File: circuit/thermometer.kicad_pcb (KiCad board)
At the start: 2 copper layers, 1 part, among them IC1 ICL7107CPL

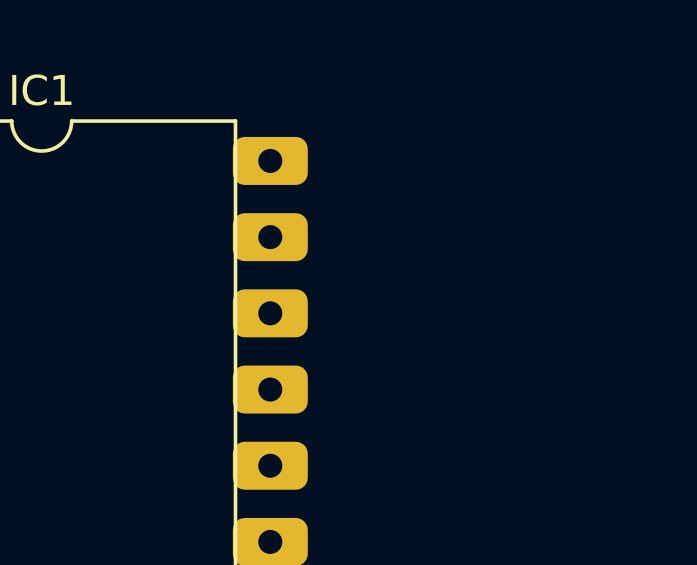
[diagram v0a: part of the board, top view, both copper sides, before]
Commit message: Configure oscillator
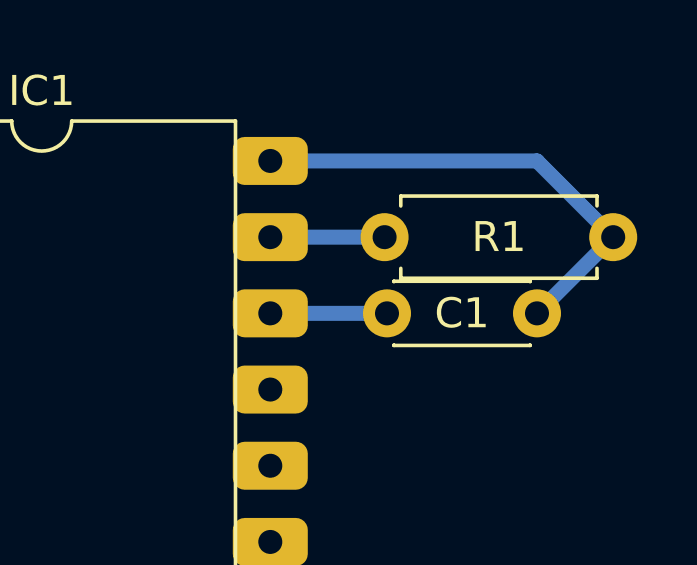
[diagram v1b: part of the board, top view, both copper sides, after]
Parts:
- added C1: 100pF, Capacitor_THT:C_Disc_D4.3mm_W1.9mm_P5.00mm, F.Cu at (101.7, 81.3)
- added R1: 100k, Resistor_THT:R_Axial_DIN0207_L6.3mm_D2.5mm_P7.62mm_Horizontal, F.Cu at (101.6, 78.7)
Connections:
- IC1 pad 38: unconnected-(IC1-OSC3-Pad38) -> Net-(IC1-OSC3)
- IC1 pad 39: unconnected-(IC1-OSC2-Pad39) -> Net-(IC1-OSC2)
- IC1 pad 40: unconnected-(IC1-OSC1-Pad40) -> Net-(IC1-OSC1)
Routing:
- net Net-(IC1-OSC1): track 0.00 -> 16.1 mm
- net Net-(IC1-OSC3): track 0.00 -> 3.89 mm
- net Net-(IC1-OSC2): track 0.00 -> 3.81 mm
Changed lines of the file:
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@@
   (net 36 "unconnected-(IC1-REF_HI-Pad36)")
   (net 37 "unconnected-(IC1-TEST-Pad37)")
-  (net 38 "unconnected-(IC1-OSC3-Pad38)")
-  (net 39 "unconnected-(IC1-OSC2-Pad39)")
-  (net 40 "unconnected-(IC1-OSC1-Pad40)")
+  (net 38 "Net-(IC1-OSC3)")
+  (net 39 "Net-(IC1-OSC1)")
+  (net 40 "Net-(IC1-OSC2)")
   (footprint "Package_DIP:DIP-40_W15.24mm" (layer "F.Cu")
     (at 82.55 76.2)
@@
       (net 37 "unconnected-(IC1-TEST-Pad37)") (pinfunction "TEST") (pintype "passive"))
     (pad "38" thru_hole roundrect (at 15.24 5.08) (size 2.5 1.6) (drill 0.8) (layers "*.Cu" "*.Mask") (roundrect_rratio 0.25)
-      (net 38 "unconnected-(IC1-OSC3-Pad38)") (pinfunction "OSC3") (pintype "passive"))
+      (net 38 "Net-(IC1-OSC3)") (pinfunction "OSC3") (pintype "passive"))
     (pad "39" thru_hole roundrect (at 15.24 2.54) (size 2.5 1.6) (drill 0.8) (layers "*.Cu" "*.Mask") (roundrect_rratio 0.25)
-      (net 39 "unconnected-(IC1-OSC2-Pad39)") (pinfunction "OSC2") (pintype "passive"))
+      (net 40 "Net-(IC1-OSC2)") (pinfunction "OSC2") (pintype "passive"))
     (pad "40" thru_hole roundrect (at 15.24 0) (size 2.5 1.6) (drill 0.8) (layers "*.Cu" "*.Mask") (roundrect_rratio 0.25)
-      (net 40 "unconnected-(IC1-OSC1-Pad40)") (pinfunction "OSC1") (pintype "passive"))
+      (net 39 "Net-(IC1-OSC1)") (pinfunction "OSC1") (pintype "passive"))
     (model "${KICAD6_3DMODEL_DIR}/Package_DIP.3dshapes/DIP-40_W15.24mm.wrl"
       (offset (xyz 0 0 0))
@@
     )
   )
+  (footprint "Capacitor_THT:C_Disc_D4.3mm_W1.9mm_P5.00mm" (layer "F.Cu")
+    (at 101.68 81.28)
+    (descr "C, Disc series, Radial, pin pitch=5.00mm, , diameter*width=4.3*1.9mm^2, Capacitor, http://www.vishay.com/docs/45233/krseries.pdf")
+    (tags "C Disc series Radial pin pitch 5.00mm  diameter 4.3mm width 1.9mm Capacitor")
+    (property "Sheetfile" "thermometer.kicad_sch")
+    (property "Sheetname" "")
+    (property "ki_description" "Unpolarized capacitor")
+    (property "ki_keywords" "cap capacitor")
+    (attr through_hole)
+    (fp_text reference "C1" (at 2.5 0) (layer "F.SilkS")
+        (effects (font (size 1 1) (thickness 0.15)))
+    )
+    (fp_text value "100pF" (at 2.5 2.2) (layer "F.Fab")
+        (effects (font (size 1 1) (thickness 0.15)))
+    )
+    (fp_text user "${REFERENCE}" (at 2.5 0) (layer "F.Fab")
+        (effects (font (size 0.86 0.86) (thickness 0.129)))
+    )
+    (fp_line (start 0.23 -1.07) (end 0.23 -1.055)
+      (stroke (width 0.12) (type solid)) (layer "F.SilkS"))
+    (fp_line (start 0.23 -1.07) (end 4.77 -1.07)
+      (stroke (width 0.12) (type solid)) (layer "F.SilkS"))
+    (fp_line (start 0.23 1.055) (end 0.23 1.07)
+      (stroke (width 0.12) (type solid)) (layer "F.SilkS"))
+    (fp_line (start 0.23 1.07) (end 4.77 1.07)
+      (stroke (width 0.12) (type solid)) (layer "F.SilkS"))
+    (fp_line (start 4.77 -1.07) (end 4.77 -1.055)
+      (stroke (width 0.12) (type solid)) (layer "F.SilkS"))
+    (fp_line (start 4.77 1.055) (end 4.77 1.07)
+      (stroke (width 0.12) (type solid)) (layer "F.SilkS"))
+    (fp_line (start -1.05 -1.2) (end -1.05 1.2)
+      (stroke (width 0.05) (type solid)) (layer "F.CrtYd"))
+    (fp_line (start -1.05 1.2) (end 6.05 1.2)
+      (stroke (width 0.05) (type solid)) (layer "F.CrtYd"))
+    (fp_line (start 6.05 -1.2) (end -1.05 -1.2)
+      (stroke (width 0.05) (type solid)) (layer "F.CrtYd"))
+    (fp_line (start 6.05 1.2) (end 6.05 -1.2)
+      (stroke (width 0.05) (type solid)) (layer "F.CrtYd"))
+    (fp_line (start 0.35 -0.95) (end 0.35 0.95)
+      (stroke (width 0.1) (type solid)) (layer "F.Fab"))
+    (fp_line (start 0.35 0.95) (end 4.65 0.95)
+      (stroke (width 0.1) (type solid)) (layer "F.Fab"))
+    (fp_line (start 4.65 -0.95) (end 0.35 -0.95)
+      (stroke (width 0.1) (type solid)) (layer "F.Fab"))
+    (fp_line (start 4.65 0.95) (end 4.65 -0.95)
+      (stroke (width 0.1) (type solid)) (layer "F.Fab"))
+    (pad "1" thru_hole circle (at 0 0) (size 1.6 1.6) (drill 0.8) (layers "*.Cu" "*.Mask")
+      (net 38 "Net-(IC1-OSC3)") (pintype "passive"))
+    (pad "2" thru_hole circle (at 5 0) (size 1.6 1.6) (drill 0.8) (layers "*.Cu" "*.Mask")
+      (net 39 "Net-(IC1-OSC1)") (pintype "passive"))
+    (model "${KICAD6_3DMODEL_DIR}/Capacitor_THT.3dshapes/C_Disc_D4.3mm_W1.9mm_P5.00mm.wrl"
+      (offset (xyz 0 0 0))
+      (scale (xyz 1 1 1))
+      (rotate (xyz 0 0 0))
+    )
+  )
+  (footprint "Resistor_THT:R_Axial_DIN0207_L6.3mm_D2.5mm_P7.62mm_Horizontal" (layer "F.Cu")
+    (at 101.6 78.74)
+    (descr "Resistor, Axial_DIN0207 series, Axial, Horizontal, pin pitch=7.62mm, 0.25W = 1/4W, length*diameter=6.3*2.5mm^2, http://cdn-reichelt.de/documents/datenblatt/B400/1_4W%23YAG.pdf")
+    (tags "Resistor Axial_DIN0207 series Axial Horizontal pin pitch 7.62mm 0.25W = 1/4W length 6.3mm diameter 2.5mm")
+    (property "Sheetfile" "thermometer.kicad_sch")
+    (property "Sheetname" "")
+    (property "ki_description" "Resistor, US symbol")
+    (property "ki_keywords" "R res resistor")
+    (attr through_hole)
+    (fp_text reference "R1" (at 3.81 0) (layer "F.SilkS")
+        (effects (font (size 1 1) (thickness 0.15)))
+    )
+    (fp_text value "100k" (at 3.81 2.37) (layer "F.Fab")
+        (effects (font (size 1 1) (thickness 0.15)))
+    )
+    (fp_text user "${REFERENCE}" (at 3.81 0) (layer "F.Fab")
+        (effects (font (size 1 1) (thickness 0.15)))
+    )
+    (fp_line (start 0.54 -1.37) (end 7.08 -1.37)
+      (stroke (width 0.12) (type solid)) (layer "F.SilkS"))
+    (fp_line (start 0.54 -1.04) (end 0.54 -1.37)
+      (stroke (width 0.12) (type solid)) (layer "F.SilkS"))
+    (fp_line (start 0.54 1.04) (end 0.54 1.37)
+      (stroke (width 0.12) (type solid)) (layer "F.SilkS"))
+    (fp_line (start 0.54 1.37) (end 7.08 1.37)
+      (stroke (width 0.12) (type solid)) (layer "F.SilkS"))
+    (fp_line (start 7.08 -1.37) (end 7.08 -1.04)
+      (stroke (width 0.12) (type solid)) (layer "F.SilkS"))
+    (fp_line (start 7.08 1.37) (end 7.08 1.04)
+      (stroke (width 0.12) (type solid)) (layer "F.SilkS"))
+    (fp_line (start -1.05 -1.5) (end -1.05 1.5)
+      (stroke (width 0.05) (type solid)) (layer "F.CrtYd"))
+    (fp_line (start -1.05 1.5) (end 8.67 1.5)
+      (stroke (width 0.05) (type solid)) (layer "F.CrtYd"))
+    (fp_line (start 8.67 -1.5) (end -1.05 -1.5)
+      (stroke (width 0.05) (type solid)) (layer "F.CrtYd"))
+    (fp_line (start 8.67 1.5) (end 8.67 -1.5)
+      (stroke (width 0.05) (type solid)) (layer "F.CrtYd"))
+    (fp_line (start 0 0) (end 0.66 0)
+      (stroke (width 0.1) (type solid)) (layer "F.Fab"))
+    (fp_line (start 0.66 -1.25) (end 0.66 1.25)
+      (stroke (width 0.1) (type solid)) (layer "F.Fab"))
+    (fp_line (start 0.66 1.25) (end 6.96 1.25)
+      (stroke (width 0.1) (type solid)) (layer "F.Fab"))
+    (fp_line (start 6.96 -1.25) (end 0.66 -1.25)
+      (stroke (width 0.1) (type solid)) (layer "F.Fab"))
+    (fp_line (start 6.96 1.25) (end 6.96 -1.25)
+      (stroke (width 0.1) (type solid)) (layer "F.Fab"))
+    (fp_line (start 7.62 0) (end 6.96 0)
+      (stroke (width 0.1) (type solid)) (layer "F.Fab"))
+    (pad "1" thru_hole circle (at 0 0) (size 1.6 1.6) (drill 0.8) (layers "*.Cu" "*.Mask")
+      (net 40 "Net-(IC1-OSC2)") (pintype "passive"))
+    (pad "2" thru_hole oval (at 7.62 0) (size 1.6 1.6) (drill 0.8) (layers "*.Cu" "*.Mask")
+      (net 39 "Net-(IC1-OSC1)") (pintype "passive"))
+    (model "${KICAD6_3DMODEL_DIR}/Resistor_THT.3dshapes/R_Axial_DIN0207_L6.3mm_D2.5mm_P7.62mm_Horizontal.wrl"
+      (offset (xyz 0 0 0))
+      (scale (xyz 1 1 1))
+      (rotate (xyz 0 0 0))
+    )
+  )
+  (segment (start 97.79 81.28) (end 101.68 81.28) (width 0.5) (layer "B.Cu") (net 38))
+  (segment (start 106.68 81.28) (end 109.22 78.74) (width 0.5) (layer "B.Cu") (net 39))
+  (segment (start 97.79 76.2) (end 106.68 76.2) (width 0.5) (layer "B.Cu") (net 39))
+  (segment (start 106.68 76.2) (end 109.22 78.74) (width 0.5) (layer "B.Cu") (net 39))
+  (segment (start 97.79 78.74) (end 101.6 78.74) (width 0.5) (layer "B.Cu") (net 40))
 )

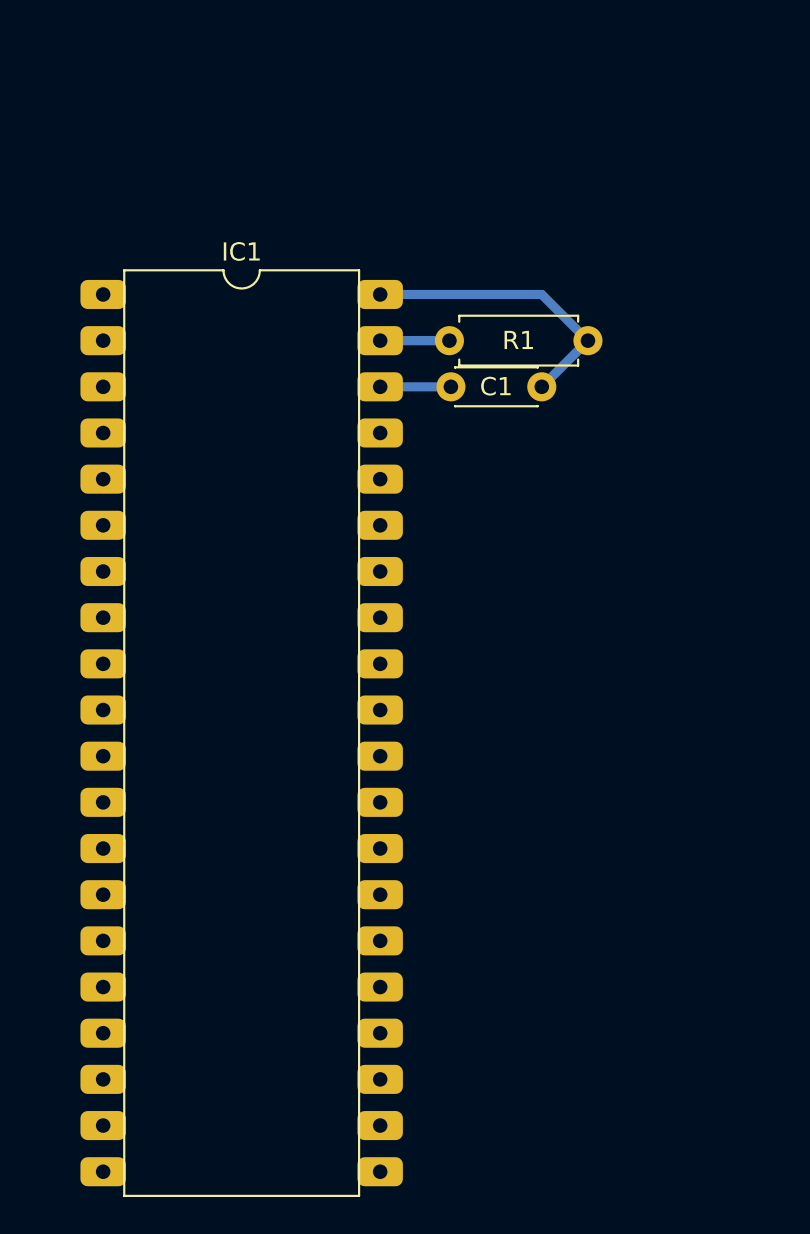
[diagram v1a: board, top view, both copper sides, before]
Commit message: Place all remaining thermometer parts
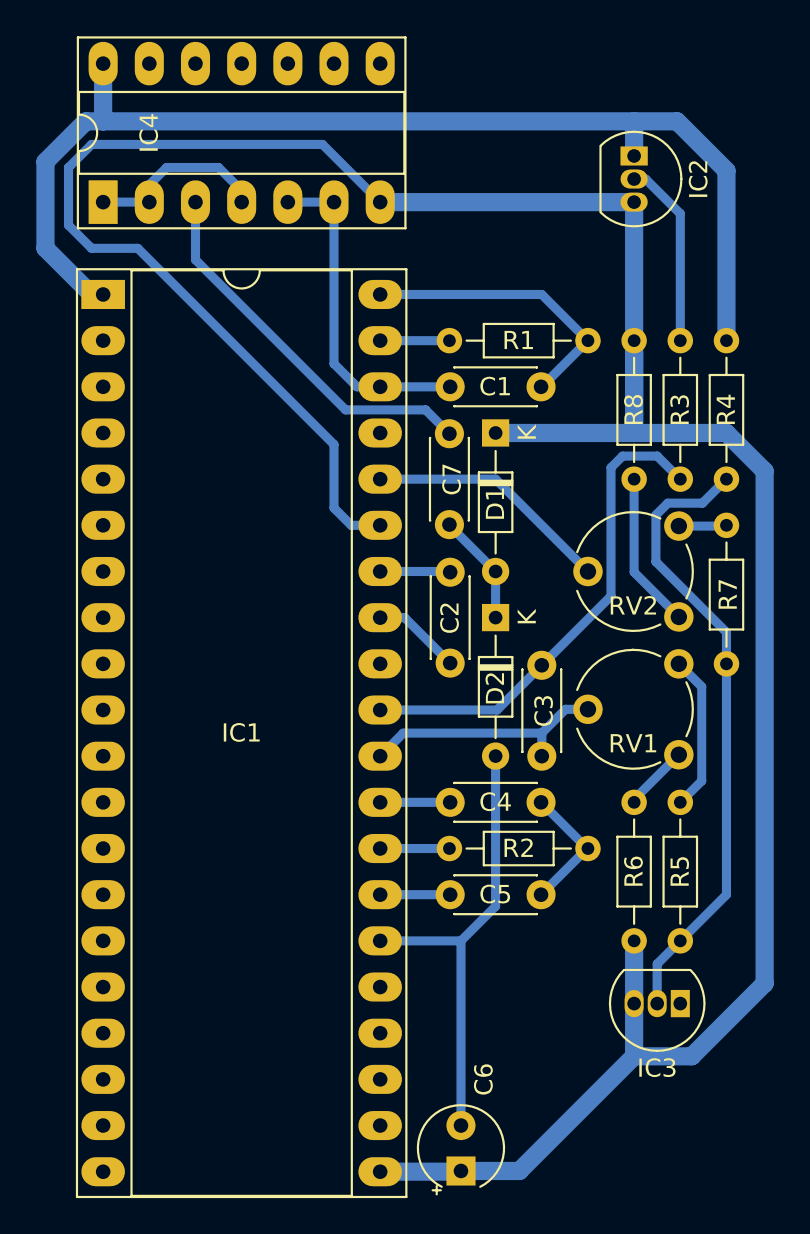
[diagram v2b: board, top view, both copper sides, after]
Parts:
- added C2: 100nF, Capacitor_THT:C_Disc_D4.3mm_W1.9mm_P5.00mm, F.Cu at (101.6, 96.5)
- added C3: 1uF, Capacitor_THT:C_Disc_D4.3mm_W1.9mm_P5.00mm, F.Cu at (106.7, 96.6)
- added C4: 470nF, Capacitor_THT:C_Disc_D4.3mm_W1.9mm_P5.00mm, F.Cu at (106.6, 104.1)
- added C5: 220nF, Capacitor_THT:C_Disc_D4.3mm_W1.9mm_P5.00mm, F.Cu at (106.6, 109.2)
- added C6: 10uF, Capacitor_THT:CP_Radial_Tantal_D4.5mm_P2.50mm, F.Cu at (102.2, 124.4)
- added C7: 47nF, Capacitor_THT:C_Disc_D4.3mm_W1.9mm_P5.00mm, F.Cu at (101.6, 88.9)
- added D1: 1N4148, Diode_THT:D_DO-34_SOD68_P7.62mm_Horizontal, F.Cu at (104.1, 83.8)
- added D2: 1N4148, Diode_THT:D_DO-34_SOD68_P7.62mm_Horizontal, F.Cu at (104.1, 94.0)
- added IC2: TMP36, Package_TO_SOT_THT:TO-92_Inline, F.Cu at (111.8, 68.6)
- added IC3: LM285Z-1.2, Package_TO_SOT_THT:TO-92_Inline, F.Cu at (114.3, 115.2)
- added IC4: 4001, Package_DIP:DIP-14_W7.62mm_Socket_LongPads, F.Cu at (82.5, 71.1)
- added R2: 47k, Resistor_THT:R_Axial_DIN0204_L3.6mm_D1.6mm_P7.62mm_Horizontal, F.Cu at (101.6, 106.7)
- added R3: 1M, Resistor_THT:R_Axial_DIN0204_L3.6mm_D1.6mm_P7.62mm_Horizontal, F.Cu at (114.3, 78.7)
- added R4: 150k, Resistor_THT:R_Axial_DIN0204_L3.6mm_D1.6mm_P7.62mm_Horizontal, F.Cu at (116.8, 78.7)
- added R5: 100k, Resistor_THT:R_Axial_DIN0204_L3.6mm_D1.6mm_P7.62mm_Horizontal, F.Cu at (114.3, 111.8)
- added R6: 68k, Resistor_THT:R_Axial_DIN0204_L3.6mm_D1.6mm_P7.62mm_Horizontal, F.Cu at (111.8, 104.1)
- added R7: 20k, Resistor_THT:R_Axial_DIN0204_L3.6mm_D1.6mm_P7.62mm_Horizontal, F.Cu at (116.8, 96.5)
- added R8: 100k, Resistor_THT:R_Axial_DIN0204_L3.6mm_D1.6mm_P7.62mm_Horizontal, F.Cu at (111.8, 86.4)
- added RV1: 10k, Potentiometer_THT:Potentiometer_Piher_PT-6-V_Vertical, F.Cu at (114.2, 96.5)
- added RV2: 10k, Potentiometer_THT:Potentiometer_Piher_PT-6-V_Vertical, F.Cu at (114.2, 88.9)
- IC1: footprint Package_DIP:DIP-40_W15.24mm -> Package_DIP:DIP-40_W15.24mm_Socket_LongPads
- R1: footprint Resistor_THT:R_Axial_DIN0207_L6.3mm_D2.5mm_P7.62mm_Horizontal -> Resistor_THT:R_Axial_DIN0204_L3.6mm_D1.6mm_P7.62mm_Horizontal
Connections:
- IC1 pad 1: unconnected-(IC1-V+-Pad1) -> +5V
- IC1 pad 21: unconnected-(IC1-BP/GND-Pad21) -> GND
- IC1 pad 26: unconnected-(IC1-V--Pad26) -> Net-(D2-A)
- IC1 pad 27: unconnected-(IC1-INT-Pad27) -> Net-(IC1-INT)
- IC1 pad 28: unconnected-(IC1-BUFF-Pad28) -> Net-(IC1-BUFF)
- IC1 pad 29: unconnected-(IC1-A-Z-Pad29) -> Net-(IC1-A-Z)
- IC1 pad 30: unconnected-(IC1-IN_LO-Pad30) -> Net-(IC1-IN_LO)
- IC1 pad 31: unconnected-(IC1-IN_HI-Pad31) -> Net-(IC1-IN_HI)
- IC1 pad 33: unconnected-(IC1-CREF--Pad33) -> Net-(IC1-CREF-)
- IC1 pad 34: unconnected-(IC1-CREF+-Pad34) -> Net-(IC1-CREF+)
- IC1 pad 35: unconnected-(IC1-REF_LO-Pad35) -> GND
- IC1 pad 36: unconnected-(IC1-REF_HI-Pad36) -> Net-(IC1-REF_HI)
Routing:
- net GND: track 0.00 -> 154.9 mm
- net +5V: track 0.00 -> 62.9 mm
- net Net-(IC3-K): track 0.00 -> 34.8 mm
- net Net-(IC1-IN_HI): track 0.00 -> 27.0 mm
- net Net-(D2-A): track 0.00 -> 25.6 mm
- net Net-(C7-Pad2): track 0.00 -> 21.1 mm
- net Net-(IC1-OSC3): track 3.89 -> 18.3 mm
- net Net-(IC1-IN_LO): track 0.00 -> 13.8 mm
- net Net-(IC1-REF_HI): track 0.00 -> 13.5 mm
- net Net-(IC2-V_{OUT}): track 0.00 -> 10.3 mm
- net Net-(IC4-Pad1): track 0.00 -> 10.1 mm
- net Net-(R5-Pad2): track 0.00 -> 8.63 mm
- net Net-(R8-Pad1): track 0.00 -> 8.60 mm
- net Net-(C4-Pad1): track 0.00 -> 7.18 mm
- net Net-(D1-A): track 0.00 -> 6.17 mm
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
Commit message: Place remaining parts
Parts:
- added DISP1: RS 587-967, Display_7Segment:7SegmentLED_LTS6760_LTS6780, F.Cu at (104.8, 120.0)
- added DISP2: D512HDB, Display_7Segment:DA56-11SURKWA, F.Cu at (104.7, 104.8)
- added DISP3: SA56-11HDB, Display_7Segment:7SegmentLED_LTS6760_LTS6780, F.Cu at (104.8, 79.4)
- added J1: Conn_01x25_Socket, Connector_PinSocket_2.54mm:PinSocket_1x25_P2.54mm_Vertical, B.Cu at (123.8, 64.1)
- added J2: Conn_01x25_Pin, Connector_PinHeader_2.54mm:PinHeader_1x25_P2.54mm_Vertical, B.Cu at (114.9, 64.1)
- added R9: 620R, Resistor_THT:R_Axial_DIN0204_L3.6mm_D1.6mm_P7.62mm_Horizontal, F.Cu at (109.8, 99.7)
- moved IC1 51.5 mm to (134.0, 74.3)
- moved IC3 51.5 mm to (165.7, 113.3)
- moved IC4 51.5 mm to (134.0, 69.2)
- moved R3 51.5 mm to (165.7, 76.8)
- moved R5 51.5 mm to (165.7, 109.9)
- moved C3 51.5 mm to (158.1, 94.7)
- moved C7 51.5 mm to (153.0, 87.0)
- moved R1 51.5 mm to (153.0, 76.8)
- moved R2 51.5 mm to (153.0, 104.8)
- moved R4 51.5 mm to (168.3, 76.8)
- moved R7 51.5 mm to (168.3, 94.6)
- moved RV1 51.5 mm to (165.7, 94.6)
- moved RV2 51.5 mm to (165.7, 87.0)
- moved C1 51.5 mm to (153.1, 79.4)
- moved C2 51.5 mm to (153.1, 94.6)
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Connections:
- IC1 pad 10: unconnected-(IC1-C2-Pad10) -> Net-(IC1-C2)
- IC1 pad 11: unconnected-(IC1-B2-Pad11) -> Net-(IC1-B2)
- IC1 pad 12: unconnected-(IC1-A2-Pad12) -> Net-(IC1-A2)
- IC1 pad 13: unconnected-(IC1-F2-Pad13) -> Net-(IC1-F2)
- IC1 pad 14: unconnected-(IC1-E2-Pad14) -> Net-(IC1-E2)
- IC1 pad 15: unconnected-(IC1-D3-Pad15) -> Net-(IC1-D3)
- IC1 pad 16: unconnected-(IC1-B3-Pad16) -> Net-(IC1-B3)
- IC1 pad 17: unconnected-(IC1-F3-Pad17) -> Net-(IC1-F3)
- IC1 pad 18: unconnected-(IC1-E3-Pad18) -> Net-(IC1-E3)
- IC1 pad 19: unconnected-(IC1-AB4-Pad19) -> Net-(IC1-AB4)
- IC1 pad 2: unconnected-(IC1-D1-Pad2) -> Net-(IC1-D1)
- IC1 pad 20: unconnected-(IC1-POL-Pad20) -> Net-(IC1-POL)
- IC1 pad 22: unconnected-(IC1-G3-Pad22) -> Net-(IC1-G3)
- IC1 pad 23: unconnected-(IC1-A3-Pad23) -> Net-(IC1-A3)
- IC1 pad 24: unconnected-(IC1-C3-Pad24) -> Net-(IC1-C3)
- IC1 pad 25: unconnected-(IC1-G2-Pad25) -> Net-(IC1-G2)
- IC1 pad 3: unconnected-(IC1-C1-Pad3) -> Net-(IC1-C1)
- IC1 pad 4: unconnected-(IC1-B1-Pad4) -> Net-(IC1-B1)
- IC1 pad 5: unconnected-(IC1-A1-Pad5) -> Net-(IC1-A1)
- IC1 pad 6: unconnected-(IC1-F1-Pad6) -> Net-(IC1-F1)
- IC1 pad 7: unconnected-(IC1-G1-Pad7) -> Net-(IC1-G1)
- IC1 pad 8: unconnected-(IC1-E1-Pad8) -> Net-(IC1-E1)
- IC1 pad 9: unconnected-(IC1-D2-Pad9) -> Net-(IC1-D2)
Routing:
- net Net-(DISP2-ca1): track 0.00 -> 85.0 mm
- net Net-(DISP1-a): track 0.00 -> 56.6 mm
- net Net-(DISP2-d2): track 0.00 -> 49.4 mm
- net Net-(DISP2-g2): track 0.00 -> 40.3 mm
- net Net-(DISP2-f1): track 0.00 -> 36.0 mm
- net Net-(IC1-G2): track 0.00 -> 33.8 mm
- net Net-(DISP2-g1): track 0.00 -> 33.1 mm
- net Net-(DISP2-a1): track 0.00 -> 33.1 mm
- net Net-(IC1-C3): track 0.00 -> 32.3 mm
- net Net-(IC1-A3): track 0.00 -> 30.8 mm
- net Net-(IC1-G3): track 0.00 -> 29.2 mm
- net GND: track 154.9 -> 182.9 mm
- net Net-(DISP2-b1): track 0.00 -> 27.5 mm
- net Net-(DISP2-a2): track 0.00 -> 26.1 mm
- net Net-(DISP2-f2): track 0.00 -> 26.1 mm
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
